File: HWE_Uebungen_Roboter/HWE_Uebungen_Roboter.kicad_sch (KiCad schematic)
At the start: 8 parts, among them IC1 TB67H450AFNG, J1 AVR-ISP-6, SW1 SW_Omron_B3FS, SW2 SW_Omron_B3FS, SW3 SW_Omron_B3FS, U1 ATmega328-P, U2 LM317_SOT-223

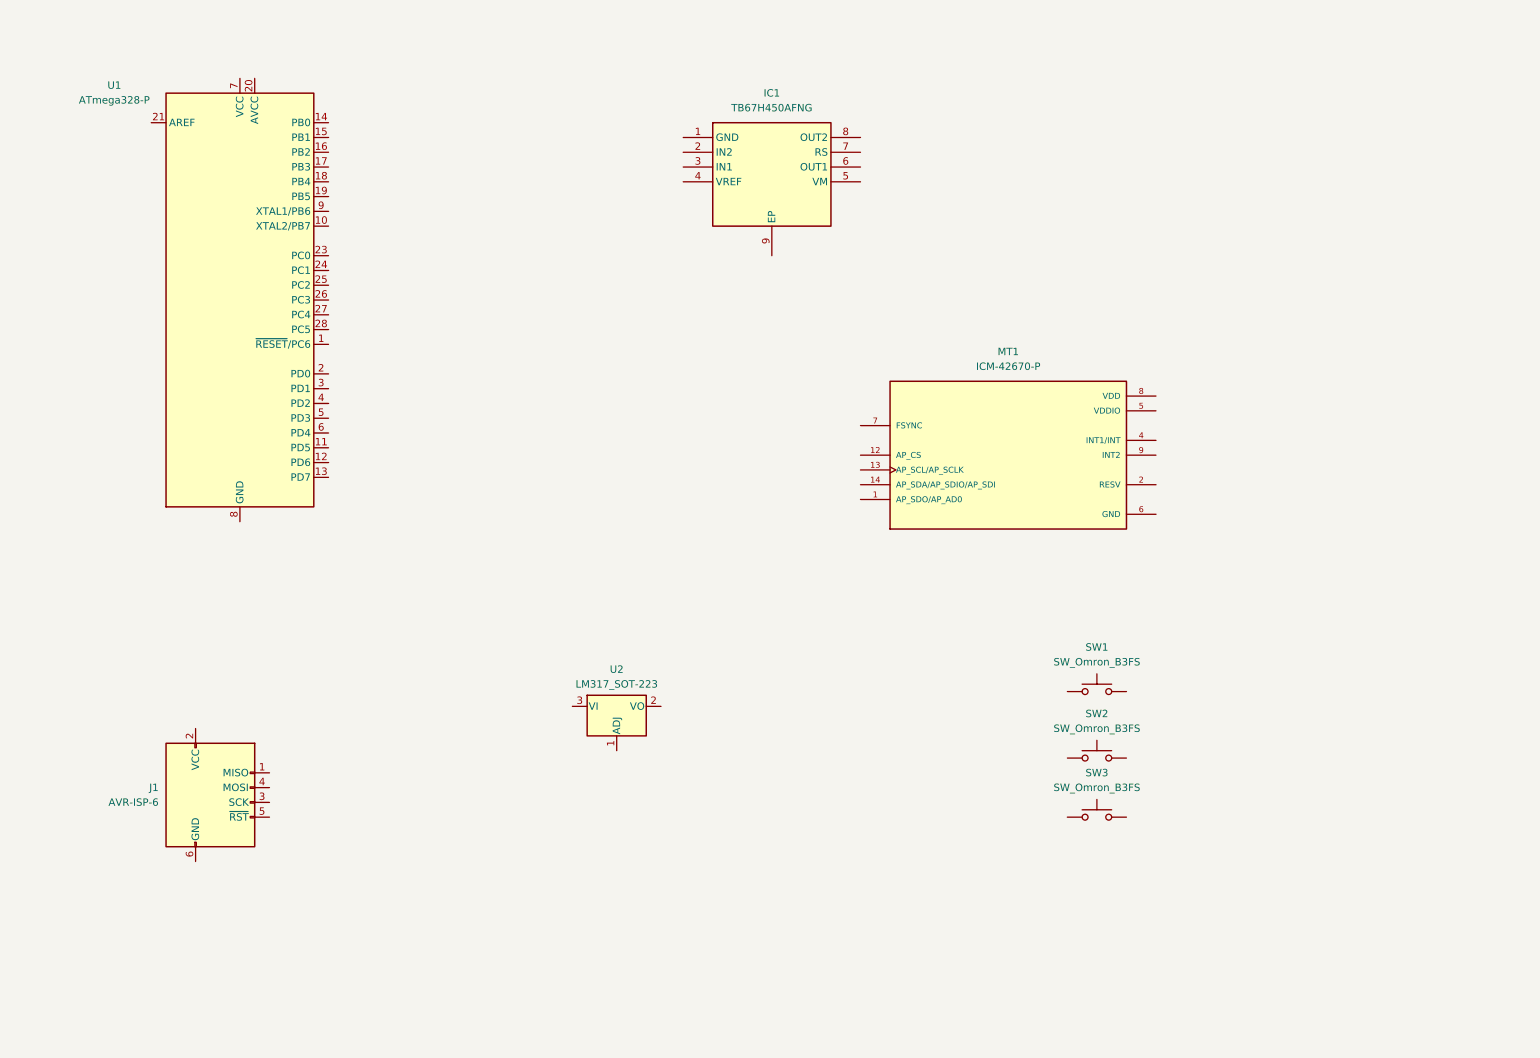
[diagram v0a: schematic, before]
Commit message: Hardware-Zwischenstand mit KiCad-Projekt und Bestückungsunterlagen
Aktuellen Hardware-Entwicklungsstand des HWE-Roboters von Felix Mähr
und Linus Kimpfler mit bestehender Projektstruktur übernehmen.

Enthalten sind:
- KiCad-Projekt mit Schaltplan und PCB-Layout
- Eigene Symbol- und Footprint-Bibliotheken mit Bibliothekstabellen
- Datenblätter der vorgesehenen Bauteile
- Schaltplan- und PCB-Abbildungen sowie 3D-Vorschau
- Interaktive HTML-Stückliste als Bestückungshilfe

Stand vor der geplanten PCB-Bestellung; das Gesamtprojekt ist noch
nicht abgeschlossen. Softwareentwicklung, Inbetriebnahme und
Funktionsnachweise sind nicht Bestandteil dieses Zwischenstands.

Die ausführliche Projektdokumentation und die .gitignore werden
in einem separaten Commit ergänzt.
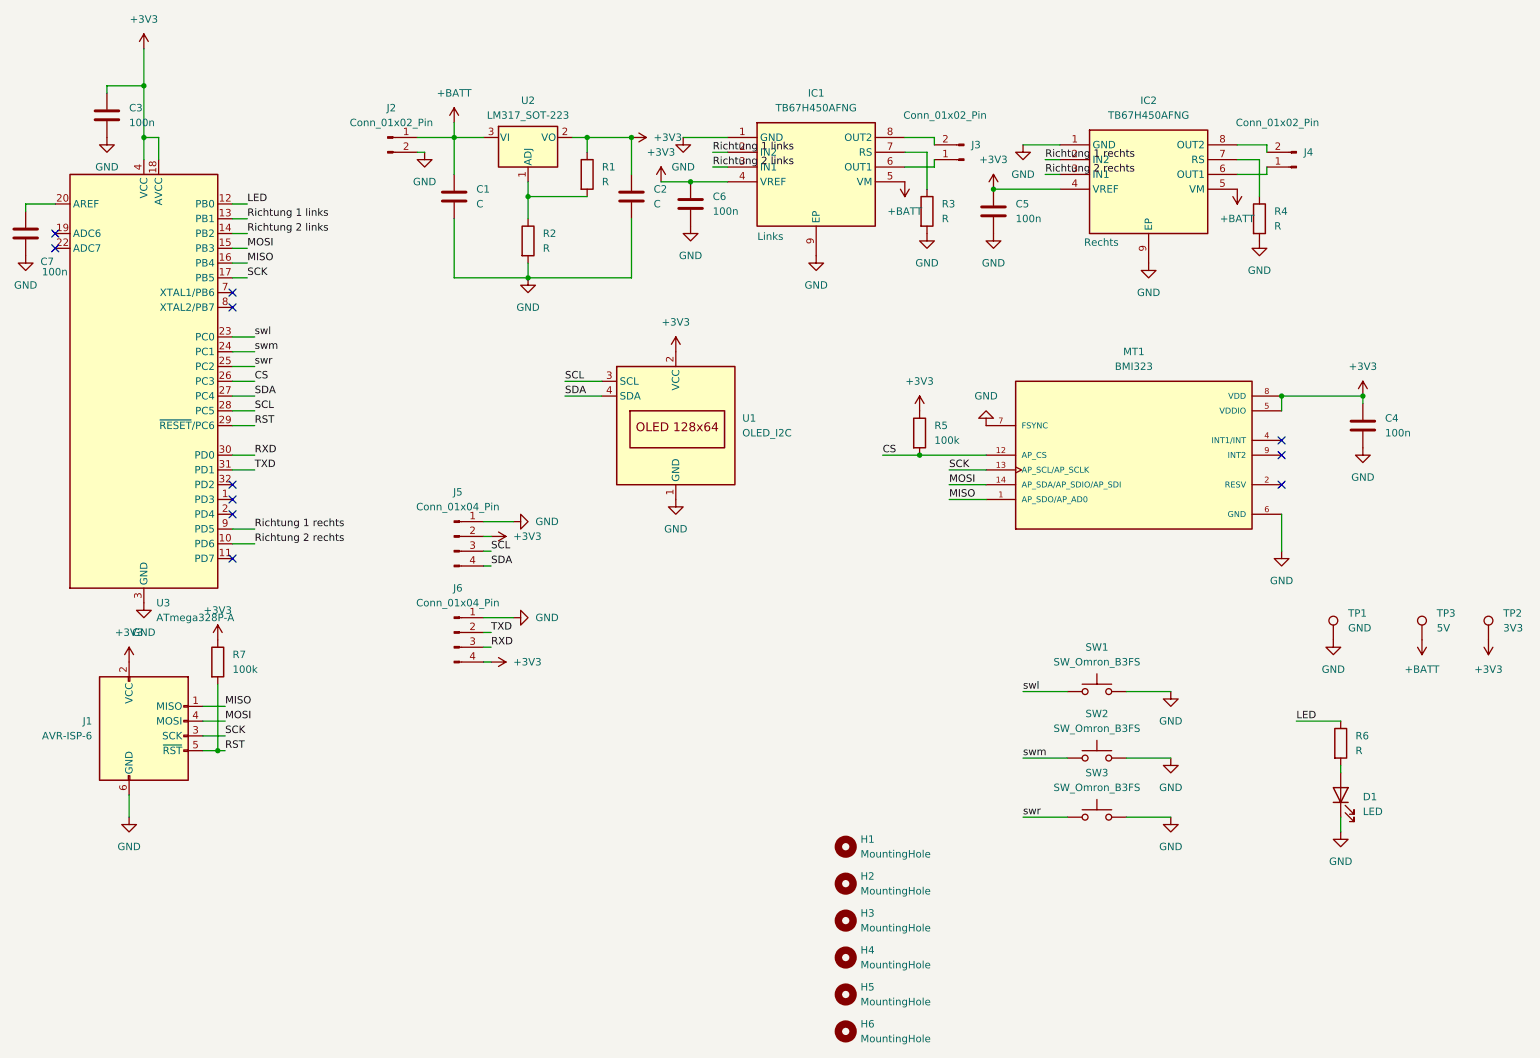
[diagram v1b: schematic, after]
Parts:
- removed U1: ATmega328-P, Package_DIP:DIP-28_W7.62mm, symbol MCU_Microchip_ATmega:ATmega328-P
- added C1, C2: C, Capacitor_SMD:C_0805_2012Metric_Pad1.18x1.45mm_HandSolder, symbol Device:C
- added C3, C4, C5, C6, C7: 100n, Capacitor_SMD:C_0805_2012Metric_Pad1.18x1.45mm_HandSolder, symbol Device:C
- added D1: LED, LED_SMD:LED_0805_2012Metric_Pad1.15x1.40mm_HandSolder, symbol Device:LED
- added H1, H2, H3, H4, H5, H6: MountingHole, MountingHole:MountingHole_3.2mm_M3, symbol Mechanical:MountingHole
- added IC2: TB67H450AFNG, Robo:P-HSOP8-0405-1.27-002, symbol Robo:TB67H450AFNG
- added J2: Conn_01x02_Pin, Connector_PinHeader_2.54mm:PinHeader_1x02_P2.54mm_Vertical, symbol Connector:Conn_01x02_Pin
- added J3, J4: Conn_01x02_Pin, Connector_Wire:SolderWire-0.5sqmm_1x02_P4.6mm_D0.9mm_OD2.1mm, symbol Connector:Conn_01x02_Pin
- added J5, J6: Conn_01x04_Pin, Connector_PinHeader_2.54mm:PinHeader_1x04_P2.54mm_Vertical, symbol Connector:Conn_01x04_Pin
- added R1, R2, R3, R4, R6: R, Resistor_SMD:R_0805_2012Metric_Pad1.20x1.40mm_HandSolder, symbol Device:R
- added R5, R7: 100k, Resistor_SMD:R_0805_2012Metric_Pad1.20x1.40mm_HandSolder, symbol Device:R
- added TP1: GND, TestPoint:TestPoint_Bridge_Pitch5.08mm_Drill0.7mm, symbol Connector:TestPoint
- added TP2: 3V3, TestPoint:TestPoint_Pad_2.0x2.0mm, symbol Connector:TestPoint
- added TP3: 5V, TestPoint:TestPoint_Pad_2.0x2.0mm, symbol Connector:TestPoint
- added U1: OLED_I2C, Robo:OLED_SSD1306_I2C_0.96, symbol LibreSolar:OLED_I2C
- added U3: ATmega328P-A, Package_QFP:TQFP-32_7x7mm_P0.8mm, symbol MCU_Microchip_ATmega:ATmega328P-A
- MT1: value ICM-42670-P -> BMI323
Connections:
- net swr: now reaches SW3.1
- net swr: now also U3.25 (PC2)
- net GND: now reaches SW3.2
- net GND: now also IC1.1 (GND), IC1.9 (EP), J1.6 (GND), MT1.6 (GND), MT1.7 (FSYNC), SW1.2, SW2.2, C1.2, C2.2, C3.2, C4.2, C5.2, C6.2, C7.2, D1.1 (K), IC2.1 (GND), IC2.9 (EP), J2.2 (Pin_2), J5.1 (Pin_1), J6.1 (Pin_1), R2.2, R3.2, R4.2, TP1.1, U1.1 (GND), U3.21 (GND), U3.3 (GND), U3.5 (GND)
- net Richtung 1 links: now reaches IC1.2 (IN2)
- net Richtung 1 links: now also U3.13 (PB1)
- net Richtung 2 links: now reaches IC1.3 (IN1)
- net Richtung 2 links: now also U3.14 (PB2)
- net +3V3: now reaches IC1.4 (VREF)
- net +3V3: now also J1.2 (VCC), MT1.5 (VDDIO), MT1.8 (VDD), U2.2 (VO), C2.1, C3.1, C4.1, C5.1, C6.1, IC2.4 (VREF), J5.2 (Pin_2), J6.4 (Pin_4), R1.1, R5.1, R7.1, TP2.1, U1.2 (VCC), U3.18 (AVCC), U3.4 (VCC), U3.6 (VCC)
- net +BATT: now reaches IC1.5 (VM)
- net +BATT: now also U2.3 (VI), C1.1, IC2.5 (VM), J2.1 (Pin_1), TP3.1
- net at IC1.6 (OUT1): now also J3.1 (Pin_1)
- net at IC1.7 (RS): now also R3.1
- net at IC1.8 (OUT2): now also J3.2 (Pin_2)
- net MISO: now reaches MT1.1 (AP_SDO/AP_AD0)
- net MISO: now also J1.1 (MISO), U3.16 (PB4)
- net CS: now reaches MT1.12 (AP_CS)
- net CS: now also R5.2, U3.26 (PC3)
- net SCK: now reaches MT1.13 (AP_SCL/AP_SCLK)
- net SCK: now also J1.3 (SCK), U3.17 (PB5)
- net MOSI: now reaches MT1.14 (AP_SDA/AP_SDIO/AP_SDI)
- net MOSI: now also J1.4 (MOSI), U3.15 (PB3)
- net swm: now reaches SW2.1
- net swm: now also U3.24 (PC1)
- net RST: now reaches J1.5 (~{RST})
- net RST: now also R7.2, U3.29 (~{RESET}/PC6)
- net at U2.1 (ADJ): now also R1.2, R2.1
- net swl: now reaches SW1.1
- net swl: now also U3.23 (PC0)
- new net: D1.2 (A), R6.2
- new net: IC2.7 (RS), R4.1
- new net: IC2.6 (OUT1), J4.1 (Pin_1)
- new net: IC2.8 (OUT2), J4.2 (Pin_2)
- new net: C7.1, U3.20 (AREF)
- new net LED: R6.1, U3.12 (PB0)
- new net RXD: J6.3 (Pin_3), U3.30 (PD0)
- new net Richtung 1 rechts: IC2.2 (IN2), U3.9 (PD5)
- new net Richtung 2 rechts: IC2.3 (IN1), U3.10 (PD6)
- new net SCL: J5.3 (Pin_3), U1.3 (SCL), U3.28 (PC5)
- new net SDA: J5.4 (Pin_4), U1.4 (SDA), U3.27 (PC4)
- new net TXD: J6.2 (Pin_2), U3.31 (PD1)
- no-connect marks 0 -> 11
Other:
- moved on the sheet: IC1, J1, MT1, U2
